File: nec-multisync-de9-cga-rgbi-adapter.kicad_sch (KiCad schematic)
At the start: 8 parts, among them J1 DE9_Plug, J2 DE15_Receptacle_HighDensity, J3 DIN-8

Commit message: Prepare to flip DIN
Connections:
- net P6_G: no longer names the net of J3.6, JP6.2 (B)
- net P6_Hs: no longer names the net of J3.5, JP5.2 (B)
- net P6_I: no longer names the net of J3.1, JP1.1 (A)
- net P6_R: no longer names the net of J3.7, JP7.1 (A)
- net P6_Vs: no longer names the net of J3.4, JP4.1 (A)
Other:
- note added: "TODO: I do NOT think we need to flip this, pin 6 on cable is the same on both ends, NOT flipped"
- note removed: "TODO: This does not work on MultiSync 3D yet (no wakeup)"
- moved on the sheet: JP1, JP4
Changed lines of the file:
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@@
   (junction (at 122.555 67.31) (diameter 0) (color 0 0 0 0)
   )
-  (junction (at 99.695 69.85) (diameter 0) (color 0 0 0 0)
+  (junction (at 97.155 69.85) (diameter 0) (color 0 0 0 0)
   )
   (junction (at 137.795 77.47) (diameter 0) (color 0 0 0 0)
@@
     (stroke (width 0) (type default))
   )
-  (wire (pts (xy 56.515 69.85) (xy 99.695 69.85))
+  (wire (pts (xy 114.935 32.385) (xy 97.155 32.385))
     (stroke (width 0) (type default))
   )
@@
     (stroke (width 0) (type default))
   )
-  (wire (pts (xy 99.695 69.85) (xy 166.37 69.85))
+  (wire (pts (xy 97.155 32.385) (xy 97.155 48.26))
     (stroke (width 0) (type default))
   )
@@
     (stroke (width 0) (type default))
   )
+  (wire (pts (xy 102.87 34.925) (xy 94.615 34.925))
+    (stroke (width 0) (type default))
+  )
   (wire (pts (xy 182.245 67.31) (xy 182.245 89.535))
     (stroke (width 0) (type default))
@@
     (stroke (width 0) (type default))
   )
+  (wire (pts (xy 97.155 58.42) (xy 97.155 69.85))
+    (stroke (width 0) (type default))
+  )
   (wire (pts (xy 164.465 82.55) (xy 164.465 132.715))
     (stroke (width 0) (type default))
@@
     (stroke (width 0) (type default))
   )
-  (wire (pts (xy 106.045 32.385) (xy 114.935 32.385))
-    (stroke (width 0) (type default))
-  )
-  (wire (pts (xy 106.045 46.99) (xy 106.045 32.385))
+  (wire (pts (xy 97.155 69.85) (xy 166.37 69.85))
     (stroke (width 0) (type default))
   )
@@
     (stroke (width 0) (type default))
   )
-  (wire (pts (xy 106.045 57.15) (xy 99.695 57.15))
-    (stroke (width 0) (type default))
-  )
   (wire (pts (xy 224.79 132.715) (xy 224.79 99.695))
     (stroke (width 0) (type default))
@@
     (stroke (width 0) (type default))
   )
-  (wire (pts (xy 99.695 57.15) (xy 99.695 69.85))
-    (stroke (width 0) (type default))
-  )
   (wire (pts (xy 210.82 99.695) (xy 224.79 99.695))
     (stroke (width 0) (type default))
@@
     (stroke (width 0) (type default))
   )
-  (wire (pts (xy 114.935 34.925) (xy 104.775 34.925))
+  (wire (pts (xy 114.935 34.925) (xy 113.03 34.925))
     (stroke (width 0) (type default))
   )
@@
     (stroke (width 0) (type default))
   )
+  (wire (pts (xy 56.515 69.85) (xy 97.155 69.85))
+    (stroke (width 0) (type default))
+  )
   (text "MultiSync Monitor" (at 193.675 119.38 0)
     (effects (font (size 1.27 1.27)) (justify left bottom))
   )
-  (text "TODO: This does not work on MultiSync 3D yet (no wakeup)"
-    (at 92.71 131.445 0)
-    (effects (font (size 1.27 1.27)) (justify left bottom))
-  )
   (text "From Japanese PC" (at 23.495 38.735 0)
     (effects (font (size 1.27 1.27)) (justify left bottom))
   )
+  (text "TODO: I do NOT think we need to flip this,\npin 6 on cable is the same on both ends, NOT flipped"
+    (at 92.075 24.13 0)
+    (effects (font (size 1.27 1.27)) (justify left bottom))
+  )
   (text "NOT ACCURATE PIN NUMBERS\nFlipped from reality because we expect a male-male cable"
-    (at 93.98 22.225 0)
+    (at 93.98 19.05 0)
     (effects (font (size 1.27 1.27)) (justify left bottom))
   )
@@
     (effects (font (size 1.27 1.27)) (justify left bottom))
   )
-  (label "P6_G" (at 107.95 29.845 0) (fields_autoplaced)
-    (effects (font (size 1.27 1.27)) (justify left bottom))
-  )
   (label "EGA_Blue1" (at 59.055 74.93 0) (fields_autoplaced)
     (effects (font (size 1.27 1.27)) (justify left bottom))
@@
     (effects (font (size 1.27 1.27)) (justify left bottom))
   )
-  (label "P6_I" (at 106.045 44.45 90) (fields_autoplaced)
-    (effects (font (size 1.27 1.27)) (justify left bottom))
-  )
-  (label "P6_Hs" (at 136.525 34.925 270) (fields_autoplaced)
-    (effects (font (size 1.27 1.27)) (justify right bottom))
-  )
-  (label "P6_B" (at 122.555 24.765 0) (fields_autoplaced)
-    (effects (font (size 1.27 1.27)) (justify left bottom))
-  )
-  (label "P6_R" (at 130.175 29.845 0) (fields_autoplaced)
-    (effects (font (size 1.27 1.27)) (justify left bottom))
-  )
   (label "EGA_Red0" (at 101.6 77.47 0) (fields_autoplaced)
     (effects (font (size 1.27 1.27)) (justify left bottom))
   )
-  (label "Ground" (at 59.055 67.31 0) (fields_autoplaced)
-    (effects (font (size 1.27 1.27)) (justify left bottom))
-  )
   (label "EGA_Red1" (at 59.055 72.39 0) (fields_autoplaced)
     (effects (font (size 1.27 1.27)) (justify left bottom))
@@
   )
   (label "HSync" (at 101.6 80.01 0) (fields_autoplaced)
-    (effects (font (size 1.27 1.27)) (justify left bottom))
-  )
-  (label "P6_Vs" (at 107.95 34.925 0) (fields_autoplaced)
     (effects (font (size 1.27 1.27)) (justify left bottom))
   )
@@
     )
   )
-  (symbol (lib_id "Jumper:Jumper_2_Bridged") (at 106.045 52.07 90) (mirror x) (unit 1)
-    (in_bom yes) (on_board yes) (dnp no)
-    (property "Reference" "JP1" (at 104.14 52.07 90)
-      (effects (font (size 1.27 1.27)) (justify left))
-    )
-    (property "Value" "Jumper_2_Bridged" (at 104.14 53.34 90)
+  (symbol (lib_id "Jumper:Jumper_2_Bridged") (at 97.155 53.34 270) (unit 1)
+    (in_bom yes) (on_board yes) (dnp no) (fields_autoplaced)
+    (property "Reference" "JP1" (at 99.06 53.34 90)
+      (effects (font (size 1.27 1.27)) (justify left))
+    )
+    (property "Value" "Jumper_2_Bridged" (at 99.06 54.61 90)
       (effects (font (size 1.27 1.27)) (justify left) hide)
     )
-    (property "Footprint" "Jumper:SolderJumper-2_P1.3mm_Bridged_Pad1.0x1.5mm" (at 106.045 52.07 0)
-      (effects (font (size 1.27 1.27)) hide)
-    )
-    (property "Datasheet" "~" (at 106.045 52.07 0)
+    (property "Footprint" "Jumper:SolderJumper-2_P1.3mm_Bridged_Pad1.0x1.5mm" (at 97.155 53.34 0)
+      (effects (font (size 1.27 1.27)) hide)
+    )
+    (property "Datasheet" "~" (at 97.155 53.34 0)
       (effects (font (size 1.27 1.27)) hide)
     )
@@
     )
   )
-  (symbol (lib_id "Jumper:Jumper_2_Bridged") (at 99.695 34.925 180) (unit 1)
+  (symbol (lib_id "Jumper:Jumper_2_Bridged") (at 107.95 34.925 180) (unit 1)
     (in_bom yes) (on_board yes) (dnp no)
-    (property "Reference" "JP4" (at 99.695 38.1 0)
+    (property "Reference" "JP4" (at 107.95 38.1 0)
       (effects (font (size 1.27 1.27)))
     )
-    (property "Value" "Jumper_2_Bridged" (at 99.695 31.75 0)
-      (effects (font (size 1.27 1.27)) hide)
-    )
-    (property "Footprint" "Jumper:SolderJumper-2_P1.3mm_Bridged_Pad1.0x1.5mm" (at 99.695 34.925 0)
-      (effects (font (size 1.27 1.27)) hide)
-    )
-    (property "Datasheet" "~" (at 99.695 34.925 0)
-      (effects (font (size 1.27 1.27)) hide)
-    )
+    (property "Value" "Jumper_2_Bridged" (at 107.95 31.75 0)
+      (effects (font (size 1.27 1.27)) hide)
+    )
+    (property "Footprint" "Jumper:SolderJumper-2_P1.3mm_Bridged_Pad1.0x1.5mm" (at 107.95 34.925 0)
+      (effects (font (size 1.27 1.27)) hide)
+    )
+    (property "Datasheet" "~" (at 107.95 34.925 0)
+      (effects (font (size 1.27 1.27)) hide)
+    )

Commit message: World's ugliest reroute
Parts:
- renumbered JP1 to JP3
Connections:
- net EGA_Green0: now also JP7.2 (B); no longer JP6.1 (A)
- net EGA_Green1_Intensity: now also JP3.1 (A); no longer JP3.2 (B)
- net EGA_Red0: now also JP6.1 (A); no longer JP7.2 (B)
- net HSync: now also JP4.1 (A); no longer JP5.1 (A)
- net VSync: now also JP5.1 (A); no longer JP4.2 (B)
- net P6_Vs: now reaches J3.5, JP5.2 (B)
- net P6_Red: now reaches J3.6, JP6.2 (B)
- net P6_Green: now reaches J3.7, JP7.1 (A)
- net at J3.1: no longer JP3.1 (A)
- net P6_Intens: now reaches J3.3
- net P6_Intens: now also JP3.2 (B)
- net P6_Hs: now reaches J3.4
- net P6_Hs: now also JP4.2 (B); no longer JP4.1 (A)
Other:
- note added: "Assuming use of the peavey DIN8 - DIN8 cable, which connects pin 6 to pin 6 of each end of the male and does not cross over"
- note added: "P6_Blue"
- note added: "P6_Gnd"
- note removed: "NOT ACCURATE PIN NUMBERS Flipped from reality because we expect a male-male cable"
- note removed: "TODO: I do NOT think we need to flip this, pin 6 on cable is the same on both ends, NOT flipped"
- moved on the sheet: JP3, JP4, JP5, JP6, JP7

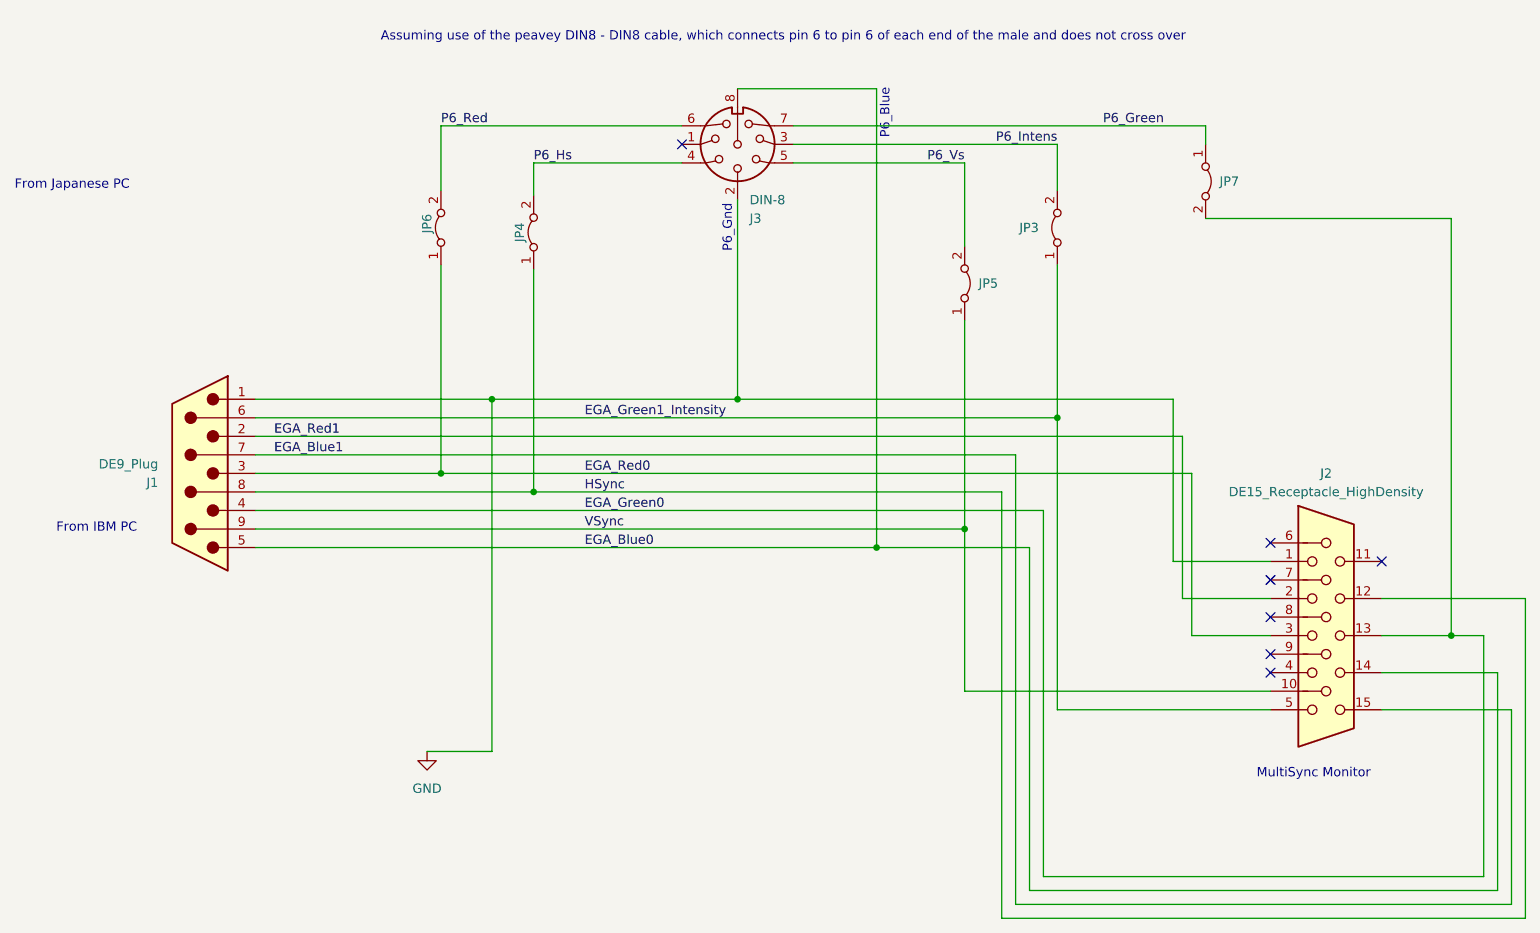
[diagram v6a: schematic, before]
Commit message: Tie shields together
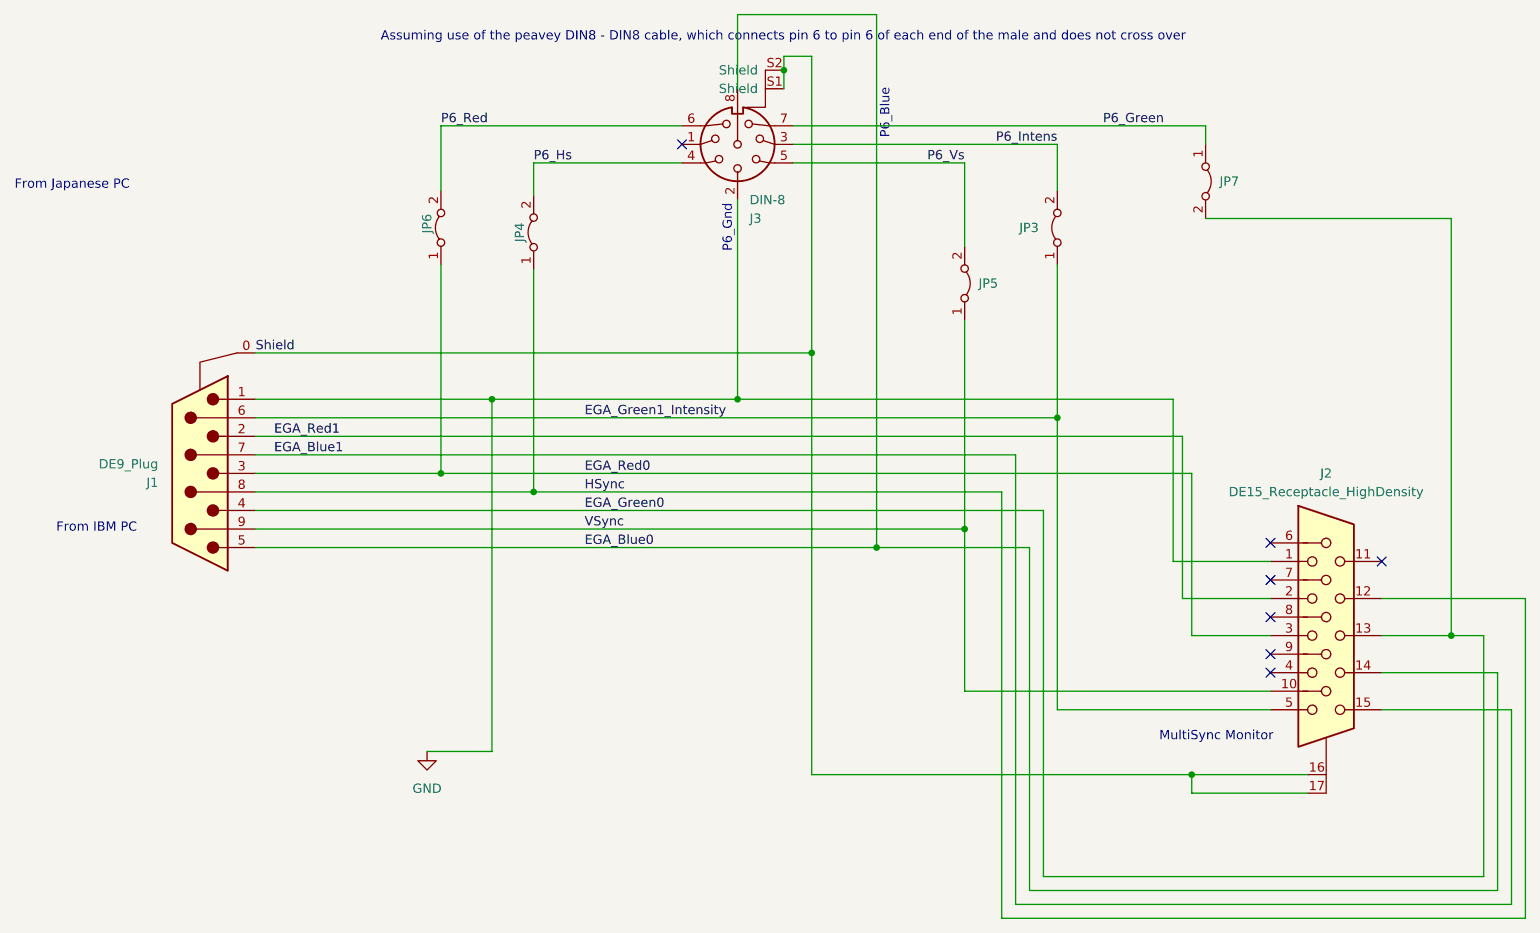
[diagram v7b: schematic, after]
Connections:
- new net Shield: J1.0 (Shield), J2.16 (Shield), J2.17 (Shield), J3.S1 (Shield), J3.S2 (Shield)
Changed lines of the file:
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@@
   (junction (at 153.67 85.09) (diameter 0) (color 0 0 0 0)
   )
+  (junction (at 184.785 118.745) (diameter 0) (color 0 0 0 0)
+  )
   (junction (at 220.345 99.695) (diameter 0) (color 0 0 0 0)
   )
@@
   )
   (junction (at 166.37 69.85) (diameter 0) (color 0 0 0 0)
+  )
+  (junction (at 128.905 22.225) (diameter 0) (color 0 0 0 0)
+  )
+  (junction (at 132.715 60.96) (diameter 0) (color 0 0 0 0)
   )
   (junction (at 122.555 67.31) (diameter 0) (color 0 0 0 0)
@@
     (stroke (width 0) (type default))
   )
+  (wire (pts (xy 184.785 118.745) (xy 132.715 118.745))
+    (stroke (width 0) (type default))
+  )
   (wire (pts (xy 186.69 42.545) (xy 220.345 42.545))
     (stroke (width 0) (type default))
@@
     (stroke (width 0) (type default))
   )
+  (wire (pts (xy 184.785 121.285) (xy 184.785 118.745))
+    (stroke (width 0) (type default))
+  )
   (wire (pts (xy 183.515 72.39) (xy 183.515 94.615))
     (stroke (width 0) (type default))
@@
     (stroke (width 0) (type default))
   )
-  (wire (pts (xy 141.605 24.765) (xy 141.605 87.63))
-    (stroke (width 0) (type default))
-  )
   (wire (pts (xy 81.915 29.845) (xy 81.915 38.735))
     (stroke (width 0) (type default))
@@
     (stroke (width 0) (type default))
   )
-  (wire (pts (xy 122.555 24.765) (xy 141.605 24.765))
+  (wire (pts (xy 128.905 22.225) (xy 128.905 20.32))
     (stroke (width 0) (type default))
   )
@@
     (stroke (width 0) (type default))
   )
+  (wire (pts (xy 132.715 20.32) (xy 132.715 60.96))
+    (stroke (width 0) (type default))
+  )
   (wire (pts (xy 228.6 109.855) (xy 210.82 109.855))
     (stroke (width 0) (type default))
@@
     (stroke (width 0) (type default))
   )
+  (wire (pts (xy 128.905 24.765) (xy 128.905 22.225))
+    (stroke (width 0) (type default))
+  )
   (wire (pts (xy 186.69 29.845) (xy 186.69 32.385))
     (stroke (width 0) (type default))
@@
     (stroke (width 0) (type default))
   )
+  (wire (pts (xy 132.715 118.745) (xy 132.715 60.96))
+    (stroke (width 0) (type default))
+  )
   (wire (pts (xy 88.9 67.31) (xy 122.555 67.31))
     (stroke (width 0) (type default))
   )
+  (wire (pts (xy 122.555 24.765) (xy 122.555 14.605))
+    (stroke (width 0) (type default))
+  )
   (wire (pts (xy 88.9 115.57) (xy 88.9 67.31))
     (stroke (width 0) (type default))
@@
     (stroke (width 0) (type default))
   )
+  (wire (pts (xy 132.715 60.96) (xy 56.515 60.96))
+    (stroke (width 0) (type default))
+  )
   (wire (pts (xy 166.37 32.385) (xy 166.37 38.735))
     (stroke (width 0) (type default))
@@
     (stroke (width 0) (type default))
   )
+  (wire (pts (xy 184.785 118.745) (xy 200.66 118.745))
+    (stroke (width 0) (type default))
+  )
   (wire (pts (xy 94.615 80.01) (xy 158.75 80.01))
     (stroke (width 0) (type default))
@@
     (stroke (width 0) (type default))
   )
+  (wire (pts (xy 128.905 20.32) (xy 132.715 20.32))
+    (stroke (width 0) (type default))
+  )
   (wire (pts (xy 122.555 40.005) (xy 122.555 67.31))
     (stroke (width 0) (type default))
@@
     (stroke (width 0) (type default))
   )
+  (wire (pts (xy 200.66 121.285) (xy 184.785 121.285))
+    (stroke (width 0) (type default))
+  )
   (wire (pts (xy 56.515 82.55) (xy 164.465 82.55))
     (stroke (width 0) (type default))
@@
     (stroke (width 0) (type default))
   )
+  (wire (pts (xy 141.605 14.605) (xy 141.605 87.63))
+    (stroke (width 0) (type default))
+  )
+  (wire (pts (xy 122.555 14.605) (xy 141.605 14.605))
+    (stroke (width 0) (type default))
+  )
   (wire (pts (xy 56.515 80.01) (xy 94.615 80.01))
     (stroke (width 0) (type default))
@@
     (stroke (width 0) (type default))
   )
-  (text "MultiSync Monitor" (at 193.675 119.38 0)
+  (text "MultiSync Monitor" (at 180.34 114.3 0)
     (effects (font (size 1.27 1.27)) (justify left bottom))
   )
@@
   )
   (label "EGA_Blue0" (at 101.6 87.63 0) (fields_autoplaced)
+    (effects (font (size 1.27 1.27)) (justify left bottom))
+  )
+  (label "Shield" (at 56.515 60.96 0) (fields_autoplaced)
     (effects (font (size 1.27 1.27)) (justify left bottom))
   )
@@
     (pin "8")
     (pin "9")
+    (pin "16")
+    (pin "17")
     (instances
       (project "nec-multisync-de9-cga-rgbi-adapter"
@@
     (pin "7")
     (pin "8")
+    (pin "S1")
+    (pin "S2")
     (instances
       (project "nec-multisync-de9-cga-rgbi-adapter"
@@
     (pin "8")
     (pin "9")
-    (instances
-      (project "nec-multisync-de9-cga-rgbi-adapter"
+    (pin "0")
+    (instances
+      (project "nec-multisync-de9-cga-rgbi-adapter"
